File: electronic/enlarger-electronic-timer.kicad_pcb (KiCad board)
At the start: 2 copper layers, 50 x 52 mm, 16 parts, among them J1 RELAY, J2 DIGIT, J3 FORCE, J4 INCREASE, J5 DECREASE, J6 TIMER, J7 USB_OTG

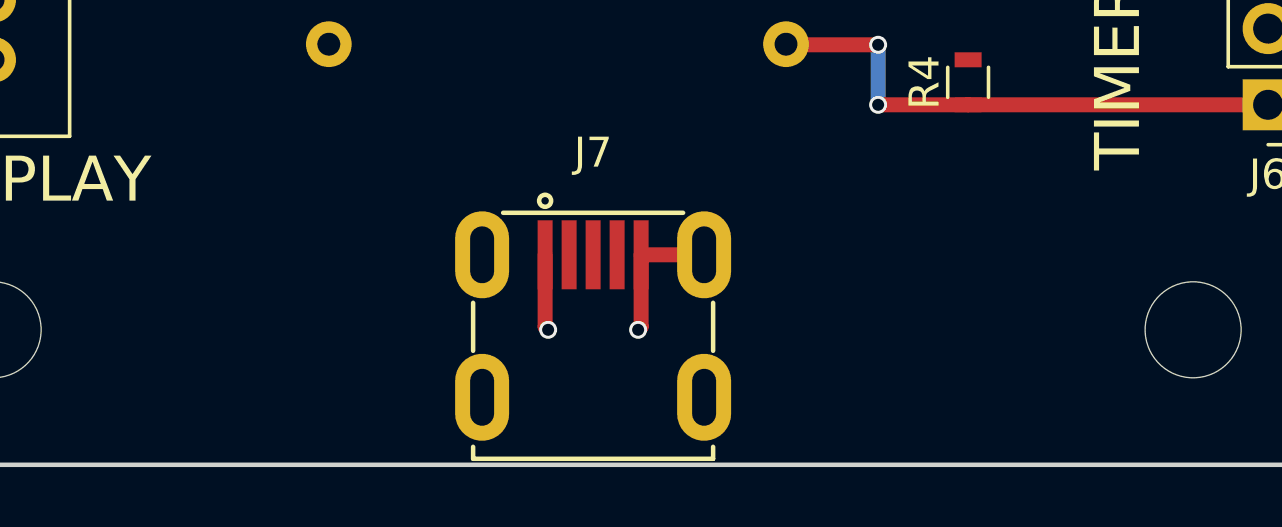
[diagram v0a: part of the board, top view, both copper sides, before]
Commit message: Added OSHW loto and PCB name. Updated plot with latest changes
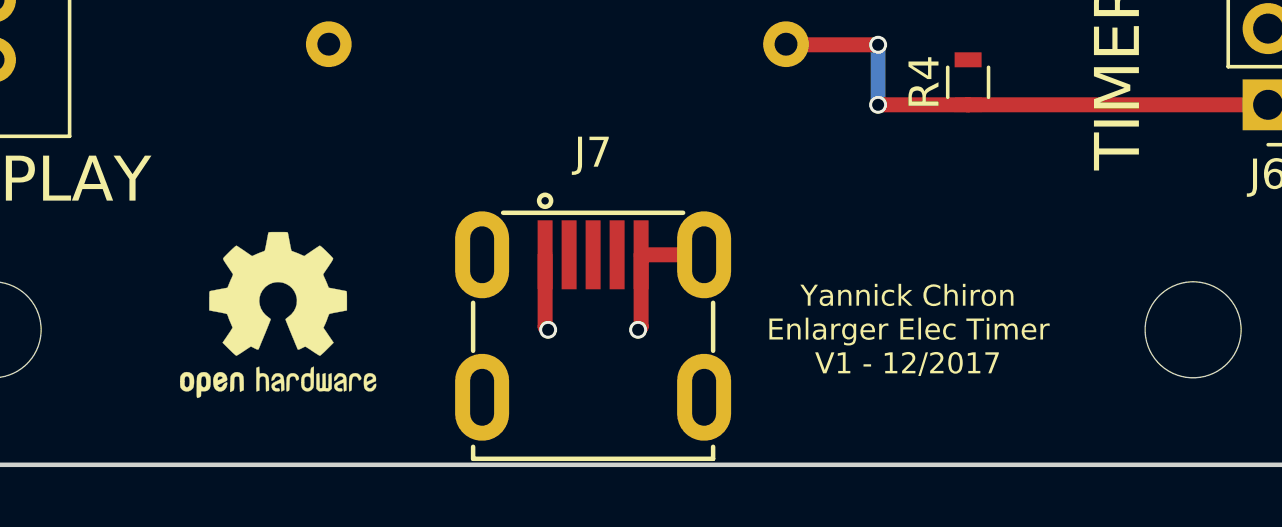
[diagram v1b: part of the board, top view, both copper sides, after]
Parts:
- added REF***: OSHW-Logo2_7.3x6mm_SilkScreen, Symbols:OSHW-Logo2_7.3x6mm_SilkScreen, F.Cu at (64.5, 97.0)
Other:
- board text added: "Yannick Chiron Enlarger Elec Timer V1 - 12/2017"
